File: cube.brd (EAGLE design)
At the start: 53.3 x 57.1 mm, 79 parts, among them Q3 DMG341, SW1 KMR2, U1 AP2112K-3.3, U2 AP2112-3.3, U3 MCP73831T-2ACI/OT, U4 2MB Flash, X1 JSTPH, X2 32.768, X3 microUSB

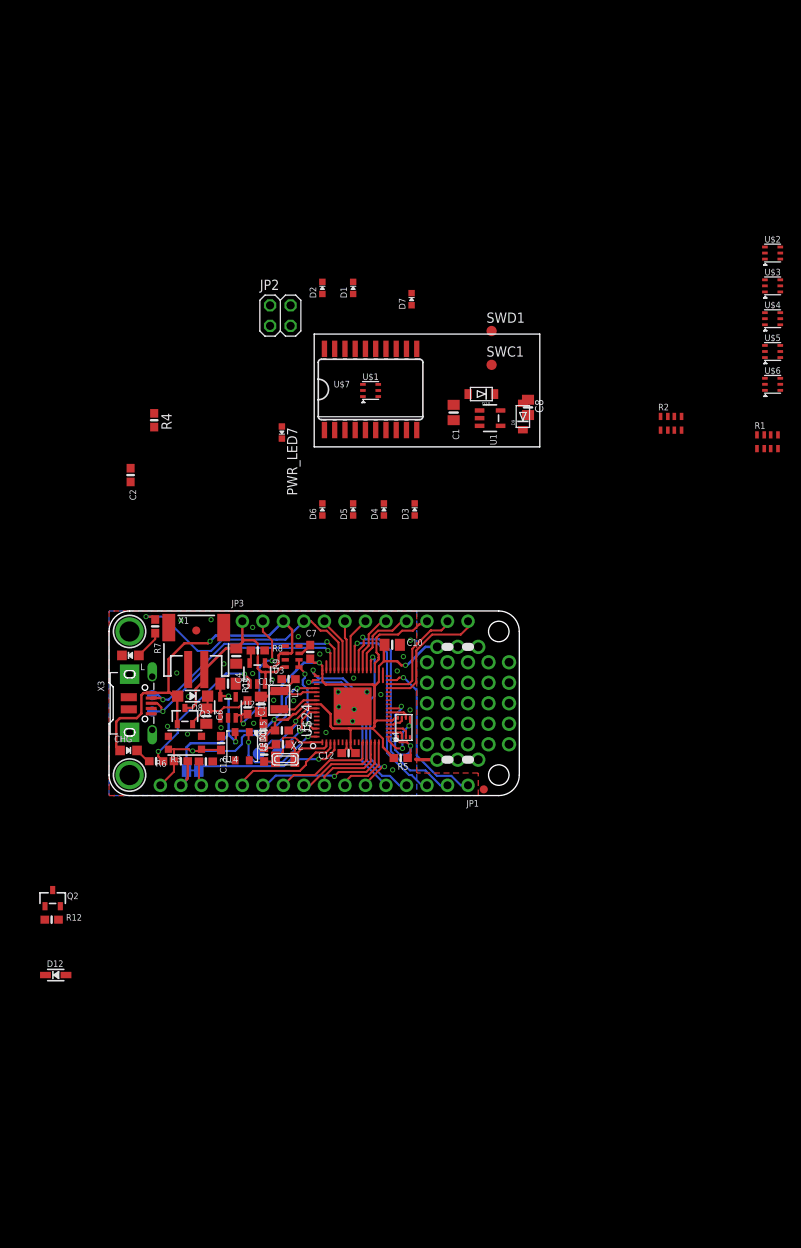
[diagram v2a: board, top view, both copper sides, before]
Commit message: adding speedypoo script, updating cube
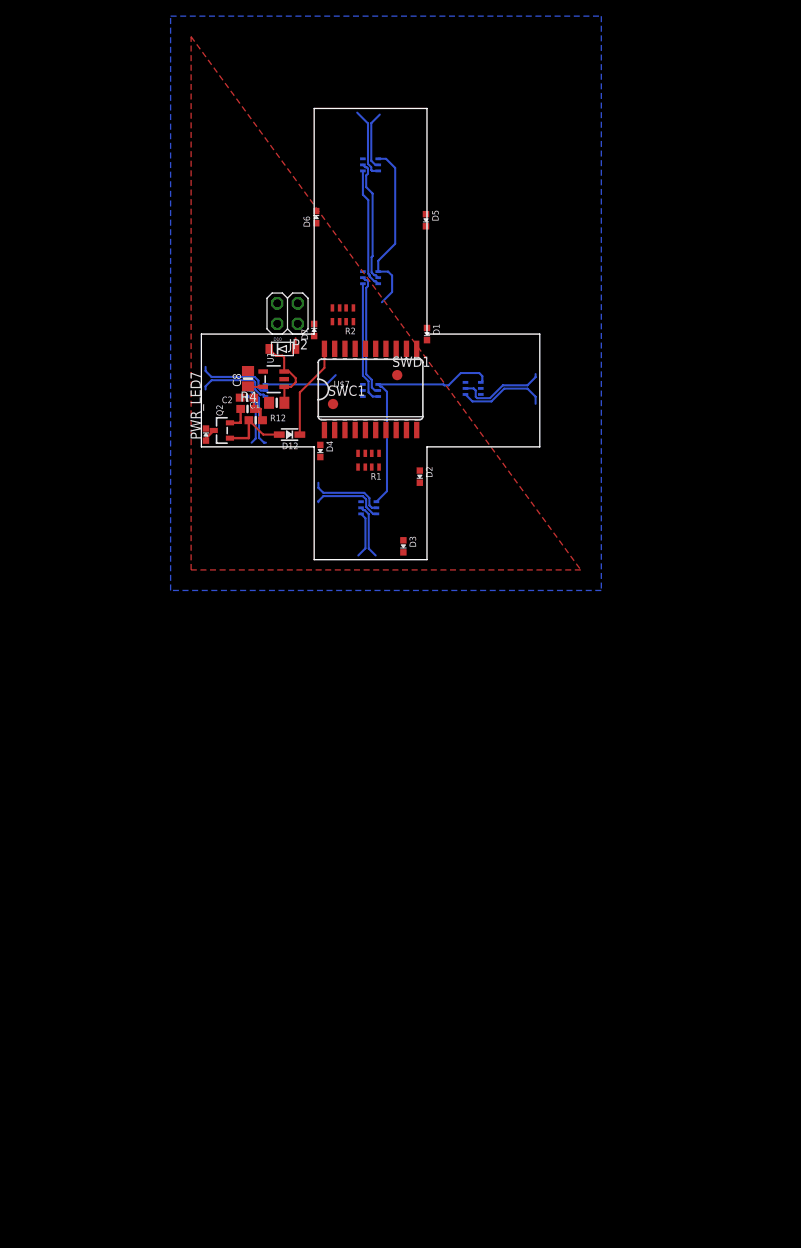
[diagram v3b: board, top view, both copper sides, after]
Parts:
- removed C10, C15: 10uF, microbuilder:0805-NO
- removed C11, C12, C13, C14, C16, C7: 1uF, microbuilder:0603-NO
- removed C3, C4, C6: 10µF, microbuilder:0805-NO
- removed C5, C9: 22pF, microbuilder:0603-NO
- removed CHG: ORANGE, microbuilder:CHIPLED_0805_NOOUTLINE
- removed D+, D-: TPB1,27, testpad:B1,27
- removed D8: MBR120, microbuilder:SOD-123
- removed D9: SCHOTTKY, adafruit:SOD-123FL
- removed JP1: (no value), microbuilder:1X16_ROUND
- removed JP3: (no value), microbuilder:1X12_ROUND
- removed L: RED, microbuilder:CHIPLED_0805_NOOUTLINE
- removed L2: 10uH, microbuilder:INDUCTOR_1007
- removed LED1: WS2812B3535, microbuilder:LED3535
- removed Q3: DMG341, microbuilder:SOT23-R
- removed R10, R11, R5, R6: 10K, microbuilder:0603-NO
- removed R3: 1K, microbuilder:0603-NO
- removed R7: 2.2K, microbuilder:0603-NO
- removed R8: 10K\, microbuilder:0603-NO
- removed R9: 100K, microbuilder:RESPACK_4X0603_NO
- removed SJ1: (no value), microbuilder:SOLDERJUMPER_CLOSEDWIRE
- removed SW1: KMR2, microbuilder:BTN_KMR2_4.6X2.8
- removed TP1, TP2: (no value), microbuilder:TESTPOINT_ROUND_1.5MM
- removed U$24: ATSAMD51J, microbuilder:PQFN64-1
- removed U$31, U$32: MOUNTINGHOLE2.5, microbuilder:MOUNTINGHOLE_2.5_PLATED
- removed U$34, U$35: FIDUCIAL_1MM, microbuilder:FIDUCIAL_1MM
- removed U$42: (no value), microbuilder:PCBFEAT-REV-040
- removed U$43: (no value), silks:FEATHERM4_BOT
- removed U$44: (no value), silks:FEATHERM4_TOP
- removed U2: AP2112-3.3, microbuilder:SOT23-5
- removed U3: MCP73831T-2ACI/OT, microbuilder:SOT23-5
- removed U4: 2MB Flash, microbuilder:USON8
- removed X1: JSTPH, microbuilder:JSTPH2
- removed X2: 32.768, adafruit2:XTAL3215
- removed X3: microUSB, microbuilder:4UCONN_20329_V2
- moved D12 72.9 mm to (-3.05, 1.52), turned to 180 degrees
- moved R12 66.8 mm to (-7.24, 3.30)
- moved U$5 63.9 mm to (-6.99, 6.99), flipped to the bottom
- moved Q2 61.6 mm to (-11.4, 2.03), turned to 90 degrees
- moved U$4 55.2 mm to (6.76, -7.54), flipped to the bottom
- moved U$3 52.0 mm to (6.99, 34.9), flipped to the bottom
- moved U$2 49.9 mm to (6.99, 21.0), flipped to the bottom
- moved R1 49.5 mm to (6.73, -1.65), turned to 180 degrees
- moved R2 42.8 mm to (3.56, 16.4), turned to 180 degrees
- moved U$6 37.1 mm to (19.7, 7.24), flipped to the bottom
- moved D5 36.9 mm to (13.8, 28.1), turned to 180 degrees
- moved D6 36.2 mm to (0.25, 28.4)
- moved C8 34.9 mm to (-8.19, 8.45), turned to 90 degrees
- moved U1 27.2 mm to (-5.02, 8.38), turned to 90 degrees
- moved D2 26.3 mm to (13.1, -3.68), turned to 180 degrees
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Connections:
- net VHI1 renamed XX
- removed net !RESET: C13.2, JP1.16, R6.2, SW1.A, SW1.A', U$24.52
- removed net +3V3: C10.1, C11.1, C12.1, C3.1, C7.1, JP1.15, LED1.2, R11.1, R5.2, R6.1, SJ1.2, U$24.16, U$24.21, U$24.34, U$24.48, U$24.56, U$24.8, U2.5, U4.8
- removed net 3.3V: C2.1
- removed net A0: JP1.12, U$24.3
- removed net A1: JP1.11, U$24.14
- removed net A2: JP1.10, U$24.11
- removed net A3: JP1.9, U$24.12
- removed net A4: JP1.8, U$24.13
- removed net A5: JP1.7, U$24.15
- removed net AREF: C14.1, JP1.14, SJ1.1, U$24.4
- removed net D+: D+.TP, U$24.46, X3.D+
- removed net D-: D-.TP, U$24.45, X3.D-
- removed net D10: JP3.7, U$24.41
- removed net D11: JP3.6, U$24.42
- removed net D12: JP3.5, U$24.43
- removed net D13: JP3.4, R7.1, U$24.44
- removed net D4: JP1.1, U$24.31
- removed net D5: JP3.10, U$24.35
- removed net D6: JP3.9, U$24.37
- removed net D8_NEOPIX: LED1.1, U$24.64
- removed net D9: JP3.8, U$24.38
- removed net DO6: U$6.1
- removed net EN: JP3.2, R10.1, U2.3
- removed net MISO: JP1.4, U$24.49
- removed net MOSI: JP1.5, U$24.50
- removed net N$1: CHG.C, R3.1
- removed net N$11: L2.P$2, U$24.55
- removed net N$2: L.A, R7.2
- removed net N$3: R3.2, U3.1
- removed net N$4: R8.1, U3.5
- removed net N$8: C5.1, U$24.1, X2.P$1
- removed net N$9: C9.1, U$24.2, X2.P$2
- removed net QSPI_CS: R5.1, U$24.24, U4.1
- removed net QSPI_DATA[0]: U$24.17, U4.5
- removed net QSPI_DATA[1]: U$24.18, U4.2
- removed net QSPI_DATA[2]: U$24.19, U4.3
- removed net QSPI_DATA[3]: U$24.20, U4.7
- removed net QSPI_SCK: U$24.23, U4.6
- removed net RX_D0: JP1.3, U$24.40
- removed net SCK: JP1.6, U$24.36
- removed net SCL: JP3.11, U$24.30
- removed net SDA: JP3.12, U$24.29
- removed net SWCLK: R11.2, TP1.P$1, U$24.57
- removed net SWDIO: TP2.P$1, U$24.58
- removed net TX_D1: JP1.2, U$24.39
- removed net VBAT: C4.1, JP3.1, Q3.3, R9.8, U3.3, X1.2
- removed net VBUS: CHG.A, D8.A, D9.A, JP3.3, Q3.1, R9.6, U3.4, X3.VBUS
- removed net VDDCORE1: C15.1, C16.1, L2.P$1, U$24.53
- removed net VHI: C6.1, D8.C, Q3.2, R10.2, U2.1
- removed net V_DIV: R9.1, R9.2, U$24.62
- net CKO1: no longer U$6.2
- net GND: no longer C10.2, C11.2, C12.2, C13.1, C14.2, C15.2, C16.2, C3.2, C4.2, C5.2, C6.2, C7.2, C9.2, JP1.13, L.C, LED1.4, R8.2, R9.3, R9.7, SW1.B, SW1.B', U$24.22, U$24.33, U$24.47, U$24.54, U$24.7, U$24.EXP, U2.2, U3.2, U4.4, X1.1, X3.BASE@1, X3.BASE@2, X3.GND, X3.SPRT@1, X3.SPRT@2, X3.SPRT@3, X3.SPRT@4
- net VDD: now also C2.1
- net VIN: no longer D9.C
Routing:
- net +3V3: track 104.9 -> 0.00 mm, vias 8 -> 0
- net VDD: track 0.00 -> 67.0 mm
- net VBUS: track 47.5 -> 0.00 mm, vias 1 -> 0
- net D13: track 33.0 -> 0.00 mm, vias 1 -> 0
- net !RESET: track 32.3 -> 0.00 mm, vias 2 -> 0
- net D-: track 30.4 -> 0.00 mm, vias 2 -> 0
- net D+: track 30.0 -> 0.00 mm, vias 2 -> 0
- net TX_D1: track 29.8 -> 0.00 mm, vias 1 -> 0
- net RX_D0: track 26.7 -> 0.00 mm, vias 1 -> 0
- net VBAT: track 25.8 -> 0.00 mm
- net AREF: track 24.5 -> 0.00 mm, vias 1 -> 0
- net MISO: track 22.8 -> 0.00 mm, vias 1 -> 0
- net CKO5: track 0.00 -> 20.6 mm
- net DO5: track 0.00 -> 20.5 mm
- net SCK: track 20.2 -> 0.00 mm, vias 2 -> 0
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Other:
- board size 53.3 x 57.1 mm -> 41.9 x 55.9 mm
